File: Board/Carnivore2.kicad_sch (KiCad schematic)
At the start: 153 parts, among them J1 Conn_01x02_Pin, T1 2SC945, T2 2SA733, T3 2SC945, T4 2SC945, T5 2SC945, T6 2SA733, U7 50 MHz, U8 DNI, X1 EDGE50/MSX, X2 HEADER_5X2, X3 HEADER_5X2

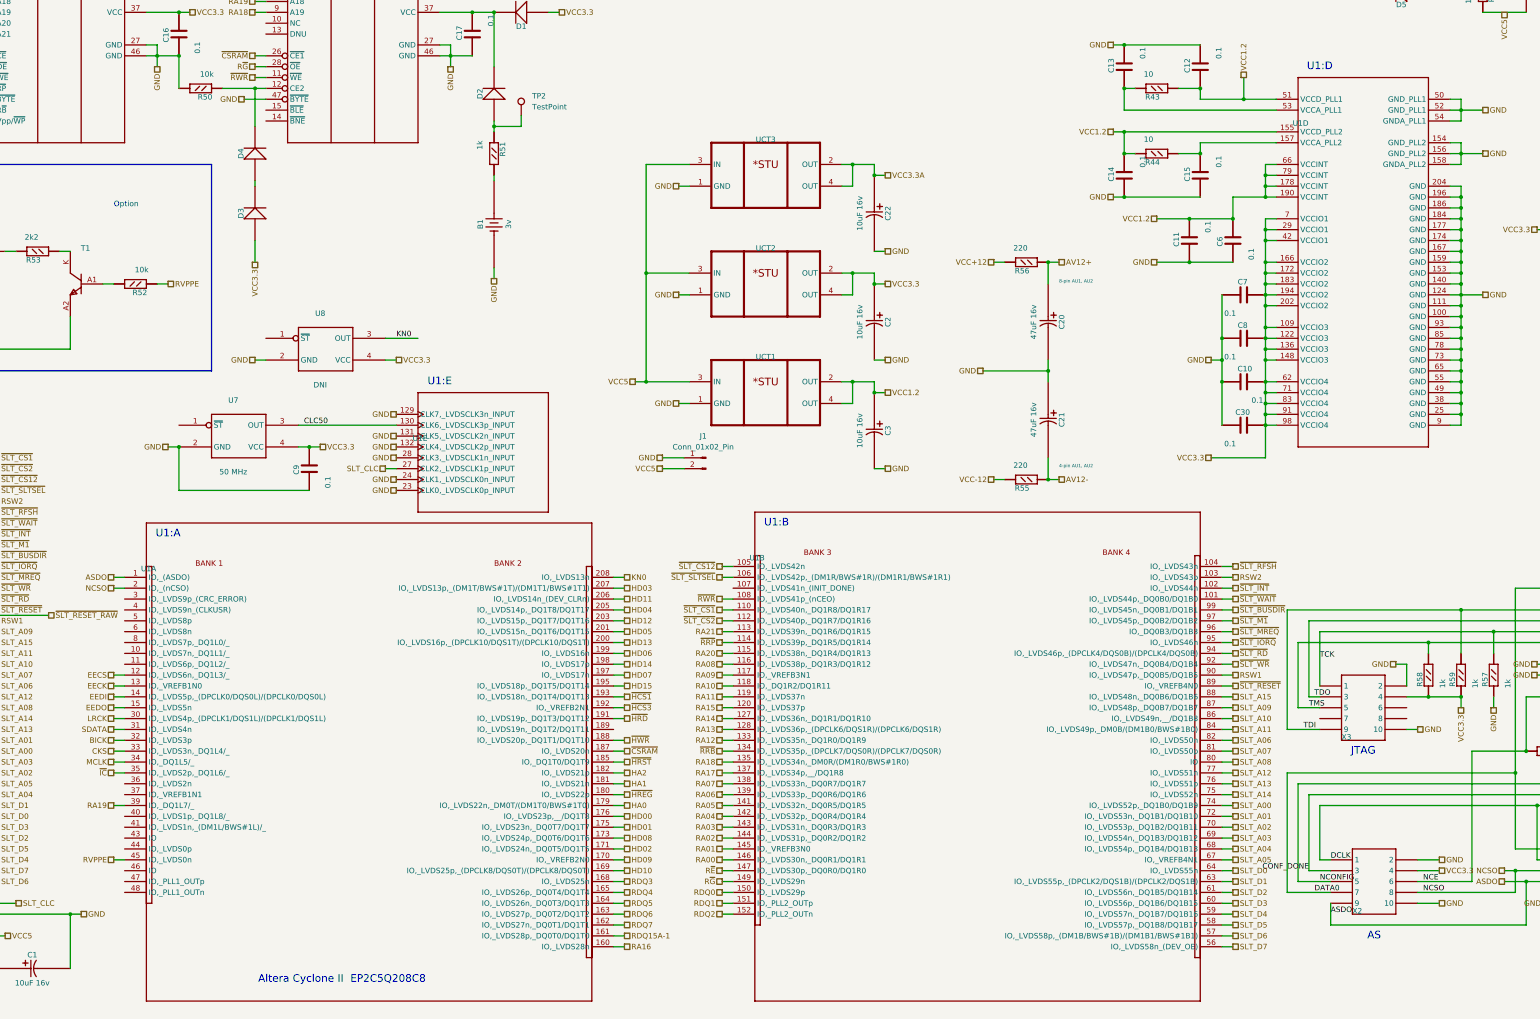
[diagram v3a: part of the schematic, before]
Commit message: Changed fpga from EP2C5 to EP2C8
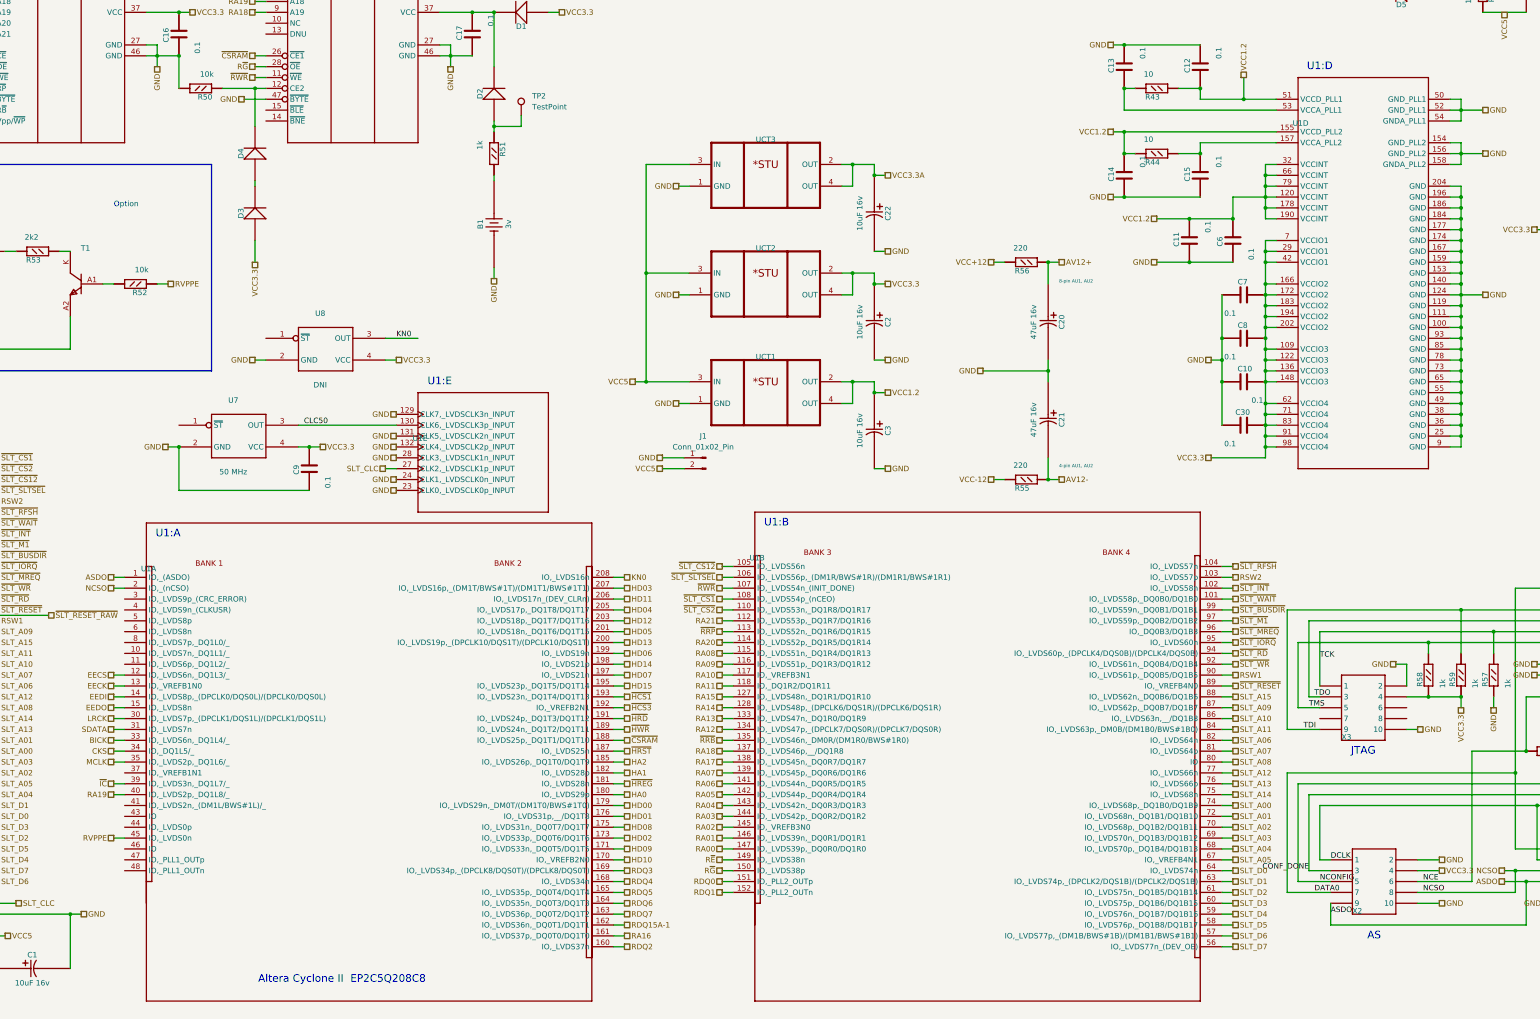
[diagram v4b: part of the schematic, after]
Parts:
- U1: footprint EP2C5Q208C8_1 -> EP2C8Q208C8_1; symbol Sheet1-altium-import:root_0_EP2C5Q208C8 -> Library:EP2C8Q208C8
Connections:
- net BICK: now also U1.33 (IO,_LVDS6n,_DQ1L4/_); no longer U1.32 (IO,_LVDS3p)
- net CKS: now also U1.34 (IO,_DQ1L5/_); no longer U1.33 (IO,_LVDS3n,_DQ1L4/_)
- net GND: now also U1.119 (GND), U1.36 (GND)
- net HA0: now also U1.180 (IO,_LVDS29p); no longer U1.179 (IO,_LVDS22n,_DM0T/(DM1T0/BWS#1T0))
- net HA1: now also U1.182 (IO,_LVDS28p); no longer U1.181 (IO,_LVDS21n)
- net HA2: now also U1.185 (IO,_LVDS26p,_DQ1T0/DQ1T9); no longer U1.182 (IO,_LVDS21p)
- net HD00: now also U1.179 (IO,_LVDS29n,_DM0T/(DM1T0/BWS#1T0)); no longer U1.176 (IO,_LVDS23p,__/DQ1T8)
- net HD01: now also U1.176 (IO,_LVDS31p,__/DQ1T8); no longer U1.175 (IO,_LVDS23n,_DQ0T7/DQ1T7)
- net HD02: now also U1.173 (IO,_LVDS33p,_DQ0T6/DQ1T6); no longer U1.171 (IO,_LVDS24n,_DQ0T5/DQ1T5)
- net HD08: now also U1.175 (IO,_LVDS31n,_DQ0T7/DQ1T7); no longer U1.173 (IO,_LVDS24p,_DQ0T6/DQ1T6)
- net HD09: now also U1.171 (IO,_LVDS33n,_DQ0T5/DQ1T5); no longer U1.170 (IO,_VREFB2N0)
- net HD10: now also U1.170 (IO,_VREFB2N0); no longer U1.169 (IO,_LVDS25p,_(DPCLK8/DQS0T)/(DPCLK8/DQS0T))
- net MCLK: now also U1.35 (IO,_LVDS2p,_DQ1L6/_); no longer U1.34 (IO,_DQ1L5/_)
- net RA00: now also U1.147 (IO,_LVDS39p,_DQ0R0/DQ1R0); no longer U1.146 (IO,_LVDS30n,_DQ0R1/DQ1R1)
- net RA01: now also U1.146 (IO,_LVDS39n,_DQ0R1/DQ1R1); no longer U1.145 (IO,_VREFB3N0)
- net RA02: now also U1.145 (IO,_VREFB3N0); no longer U1.144 (IO,_LVDS31p,_DQ0R2/DQ1R2)
- net RA03: now also U1.144 (IO,_LVDS42p,_DQ0R2/DQ1R2); no longer U1.143 (IO,_LVDS31n,_DQ0R3/DQ1R3)
- net RA04: now also U1.143 (IO,_LVDS42n,_DQ0R3/DQ1R3); no longer U1.142 (IO,_LVDS32p,_DQ0R4/DQ1R4)
- net RA05: now also U1.142 (IO,_LVDS44p,_DQ0R4/DQ1R4); no longer U1.141 (IO,_LVDS32n,_DQ0R5/DQ1R5)
- net RA06: now also U1.141 (IO,_LVDS44n,_DQ0R5/DQ1R5); no longer U1.139 (IO,_LVDS33p,_DQ0R6/DQ1R6)
- net RA07: now also U1.139 (IO,_LVDS45p,_DQ0R6/DQ1R6); no longer U1.138 (IO,_LVDS33n,_DQ0R7/DQ1R7)
- net RA08: now also U1.115 (IO,_LVDS51n,_DQ1R4/DQ1R13); no longer U1.116 (IO,_LVDS38p,_DQ1R3/DQ1R12)
- net RA09: now also U1.116 (IO,_LVDS51p,_DQ1R3/DQ1R12); no longer U1.117 (IO,_VREFB3N1)
- net RA10: now also U1.117 (IO,_VREFB3N1); no longer U1.118 (IO,_DQ1R2/DQ1R11)
- net RA11: now also U1.118 (IO,_DQ1R2/DQ1R11); no longer U1.119 (IO,_LVDS37n)
- net RA12: now also U1.134 (IO,_LVDS47p,_(DPCLK7/DQS0R)/(DPCLK7/DQS0R)); no longer U1.133 (IO,_LVDS35n,_DQ1R0/DQ1R9)
- net RA13: now also U1.133 (IO,_LVDS47n,_DQ1R0/DQ1R9); no longer U1.128 (IO,_LVDS36p,_(DPCLK6/DQS1R)/(DPCLK6/DQS1R))
- net RA14: now also U1.128 (IO,_LVDS48p,_(DPCLK6/DQS1R)/(DPCLK6/DQS1R)); no longer U1.127 (IO,_LVDS36n,_DQ1R1/DQ1R10)
- net RA15: now also U1.127 (IO,_LVDS48n,_DQ1R1/DQ1R10); no longer U1.120 (IO,_LVDS37p)
- net RA16: now also U1.161 (IO,_LVDS37p,_DQ0T0/DQ1T0); no longer U1.160 (IO,_LVDS28n)
- net RA17: now also U1.138 (IO,_LVDS45n,_DQ0R7/DQ1R7); no longer U1.137 (IO,_LVDS34p,__/DQ1R8)
- net RA18: now also U1.137 (IO,_LVDS46p,__/DQ1R8); no longer U1.135 (IO,_LVDS34n,_DM0R/(DM1R0/BWS#1R0))
- net RA19: now also U1.40 (IO,_LVDS2p,_DQ1L8/_); no longer U1.39 (IO,_DQ1L7/_)
- net RA20: now also U1.114 (IO,_LVDS52p,_DQ1R5/DQ1R14); no longer U1.115 (IO,_LVDS38n,_DQ1R4/DQ1R13)
- net RA21: now also U1.112 (IO,_LVDS53p,_DQ1R7/DQ1R16); no longer U1.113 (IO,_LVDS39n,_DQ1R6/DQ1R15)
- net RDQ0: now also U1.151 (IO,_PLL2_OUTp); no longer U1.150 (IO,_LVDS29p)
- net RDQ1: now also U1.152 (IO,_PLL2_OUTn); no longer U1.151 (IO,_PLL2_OUTp)
- net RDQ15A-1: now also U1.162 (IO,_LVDS36n,_DQ0T1/DQ1T1); no longer U1.161 (IO,_LVDS28p,_DQ0T0/DQ1T0)
- net RDQ2: now also U1.160 (IO,_LVDS37n); no longer U1.152 (IO,_PLL2_OUTn)
- net RDQ3: now also U1.169 (IO,_LVDS34p,_(DPCLK8/DQS0T)/(DPCLK8/DQS0T)); no longer U1.168 (IO,_LVDS25n)
- net RDQ4: now also U1.168 (IO,_LVDS34n); no longer U1.165 (IO,_LVDS26p,_DQ0T4/DQ1T4)
- net RDQ5: now also U1.165 (IO,_LVDS35p,_DQ0T4/DQ1T4); no longer U1.164 (IO,_LVDS26n,_DQ0T3/DQ1T3)
- net RDQ6: now also U1.164 (IO,_LVDS35n,_DQ0T3/DQ1T3); no longer U1.163 (IO,_LVDS27p,_DQ0T2/DQ1T2)
- net RDQ7: now also U1.163 (IO,_LVDS36p,_DQ0T2/DQ1T2); no longer U1.162 (IO,_LVDS27n,_DQ0T1/DQ1T1)
- net R~{E}: now also U1.149 (IO,_LVDS38n); no longer U1.147 (IO,_LVDS30p,_DQ0R0/DQ1R0)
- net R~{G}: now also U1.150 (IO,_LVDS38p); no longer U1.149 (IO,_LVDS29n)
- net VCC1.2: now also U1.120 (VCCINT), U1.32 (VCCINT)
- net ~{CSRAM}: now also U1.188 (IO,_LVDS25p,_DQ1T1/DQ1T10); no longer U1.187 (IO,_LVDS20n)
- net ~{HREG}: now also U1.181 (IO,_LVDS28n); no longer U1.180 (IO,_LVDS22p)
- net ~{HRST}: now also U1.187 (IO,_LVDS25n); no longer U1.185 (IO,_DQ1T0/DQ1T9)
- net ~{HWR}: now also U1.189 (IO,_LVDS24n,_DQ1T2/DQ1T11); no longer U1.188 (IO,_LVDS20p,_DQ1T1/DQ1T10)
- net ~{IC}: now also U1.39 (IO,_LVDS3n,_DQ1L7/_); no longer U1.35 (IO,_LVDS2p,_DQ1L6/_)
- net ~{RRB}: now also U1.135 (IO,_LVDS46n,_DM0R/(DM1R0/BWS#1R0)); no longer U1.134 (IO,_LVDS35p,_(DPCLK7/DQS0R)/(DPCLK7/DQS0R))
- net ~{RRP}: now also U1.113 (IO,_LVDS52n,_DQ1R6/DQ1R15); no longer U1.114 (IO,_LVDS39p,_DQ1R5/DQ1R14)
- net ~{RWR}: now also U1.107 (IO,_LVDS54n_(INIT_DONE)); no longer U1.108 (IO,_LVDS41p_(nCEO))
- net ~{SLT_CS1}: now also U1.108 (IO,_LVDS54p_(nCEO)); no longer U1.110 (IO,_LVDS40n,_DQ1R8/DQ1R17)
- net ~{SLT_CS2}: now also U1.110 (IO,_LVDS53n,_DQ1R8/DQ1R17); no longer U1.112 (IO,_LVDS40p,_DQ1R7/DQ1R16)

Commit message: Changed audio DAC to modern type, added audio input, updated footprints
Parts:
- removed AU1: ~, 4558D_1, symbol Sheet1-altium-import:root_2_mirrored_4558D
- removed AU2: ~, 4558D_1, symbol Sheet1-altium-import:root_0_4558D
- removed C18: 0.1mk, C_0603_1, symbol Sheet1-altium-import:root_0_C_0805
- removed C19: 0.1mk, C_0603_1, symbol Sheet1-altium-import:root_1_C_0805
- removed C20, C21: 100mk 16v, C_1812_1, symbol Sheet1-altium-import:root_3_CAP100RP
- removed C202: 1n, C_0603_1, symbol Sheet1-altium-import:root_1_C_0805
- removed D5: 1N4148, DIODE_1N4148_1, symbol Sheet1-altium-import:root_2_DIODE
- removed D6: 1N4148, DIODE_1N4148_1, symbol Sheet1-altium-import:root_1_DIODE
- removed R101, R201, R52: 10k, R_0603_1, symbol Sheet1-altium-import:root_2_R_0805
- removed R102, R202: 4.7k, R_0603_1, symbol Sheet1-altium-import:root_2_R_0805
- removed R105, R205: 1.8k, R_0603_1, symbol Sheet1-altium-import:root_2_R_0805
- removed R106, R206: 1k, R_0603_1, symbol Sheet1-altium-import:root_2_R_0805
- removed R53, R62, R63: 2.2k, R_0603_1, symbol Sheet1-altium-import:root_2_R_0805
- removed R54: 10, R_0603_1, symbol Sheet1-altium-import:root_3_R_0805
- removed R55, R56: 220, R_0603_1, symbol Sheet1-altium-import:root_2_R_0805
- removed R65: 10k, R_0603_1, symbol Sheet1-altium-import:root_3_R_0805
- removed T1: 2SC945, SOT-23(A1A2K)_1, symbol Sheet1-altium-import:root_0_mirrored_NPN
- removed T2: 2SA733, SOT-23(A1A2K)_1, symbol Sheet1-altium-import:root_2_PNP
- removed T3, T4, T5: 2SC945, SOT-23(A1A2K)_1, symbol Sheet1-altium-import:root_2_mirrored_NPN
- removed T6: 2SA733, SOT-23(A1A2K)_1, symbol Sheet1-altium-import:root_2_mirrored_PNP
- removed U5: ~, YAC516-E_1, symbol Sheet1-altium-import:root_0_YAC516-E
- removed U8: DNI, Oscillator:Oscillator_SMD_TXC_7C-4Pin_5.0x3.2mm_HandSoldering, symbol Sheet1-altium-import:root_0_SG-310
- added AX2: {Value}, Library:ST-222_1, symbol Sheet1-altium-import:root_0_mirrored_ST-222
- added C31, C32, C33, C34, C35: 100nF, Library:C_0603_1, symbol Sheet1-altium-import:root_1_C_0805
- added C36: 2.2nF, Library:C_0603_1, symbol Sheet1-altium-import:root_1_C_0805
- added J2: Conn_01x03_Pin, Connector_PinHeader_2.54mm:PinHeader_1x03_P2.54mm_Vertical, symbol Connector:Conn_01x03_Pin
- added R49: 470, Library:R_0603_1, symbol Sheet1-altium-import:root_2_R_0805
- added R99: 10, Library:R_0603_1, symbol Sheet1-altium-import:root_2_R_0805
- added U5: ~, Package_SO:TSSOP-20_4.4x6.5mm_P0.65mm, symbol Library:PCM510xA
- added U9: ~, Package_SO:TSSOP-14_4.4x5mm_P0.65mm, symbol Library:PCM1808
- AX1: footprint ST-222_1 -> Library:ST-222_1
- B1: footprint (none) -> Library:BAT
- C1, C2, C22, C3, C4: footprint C_1812_1 -> Library:C_1812_1
- C10, C11, C12, C13, C14, C15, C16, C17, C30, C5, C6, C7, C8, C9, LED1: footprint C_0603_1 -> Library:C_0603_1
- C101, C201: value 1n -> 2.2nF; footprint C_0603_1 -> Library:C_0603_1; ALTIUM_VALUE 1n -> (none)
- C102: value 1n -> 100nF; footprint C_0603_1 -> Library:C_0603_1; ALTIUM_VALUE 1n -> (none)
- C103, C105, C203, C205: value 4.7mk 25v -> 10uF 16V; footprint C_1206_1 -> Library:C_1206_1; ALTIUM_VALUE 4,7uF 25v -> (none)
- C104, C204: value 390p -> 2.2uF; footprint C_0603_1 -> Library:C_0603_1; ALTIUM_VALUE 390p -> (none)
- C23: value 10mk -> 10uF 16V; footprint C_1812_1 -> Library:C_1812_1; ALTIUM_VALUE 10uF 16v -> (none)
- C24, C25, C27: value 0.1mk -> 100nF; footprint C_0603_1 -> Library:C_0603_1; ALTIUM_VALUE 0.1 -> (none)
- C26: value 10mk -> 10uF 16V; footprint C_1812_1 -> Library:C_1812_1; ALTIUM_VALUE 10uF16v -> (none)
- C28: value 10mk -> 10uF 16v; footprint C_1812_1 -> Library:C_1812_1; ALTIUM_VALUE 10uF 10v -> (none)
- C29: value 22mk -> 10uF 16V; footprint C_1812_1 -> Library:C_1812_1; ALTIUM_VALUE 22uF 10v -> (none)
- D1, D2, D3, D4: footprint DIODE_1N4148_1 -> Library:DIODE_1N4148_1
- H1, H2: footprint (none) -> Library:MountingHole
- J1: footprint JUMPER_1 -> Library:JUMPER_1
- R10, R11, R12, R13, R14, R15, R16, R17, R18, R19, R2, R20, R21, R22, R23, R24, R25, R26, R27, R28, R29, R3, R30, R31, R32, R33, R34, R35, R36, R37, R38, R39, R4, R40, R41, R42, R5, R6, R7, R8, R9: footprint C0603_1 -> Library:R_0603_1
- R103, R203, R43, R44, R45, R46, R47, R48, R50, R51, R57, R58, R59, R64, R66: footprint R_0603_1 -> Library:R_0603_1
- R104, R204: value 100k -> 470; footprint R_0603_1 -> Library:R_0603_1; ALTIUM_VALUE 100k -> (none)
- R60: value 10k -> 470; footprint R_0603_1 -> Library:R_0603_1; ALTIUM_VALUE 10K -> (none)
- R61: value 2.2k -> 470; footprint R_0603_1 -> Library:R_0603_1; ALTIUM_VALUE 2k2 -> (none)
- TP1, TP2: footprint (none) -> Library:TestPoint_THTPad_D1.5mm_Drill0.9mm
- U1: footprint EP2C8Q208C8_1 -> Library:EP2C5Q208C8_1
- U2: footprint M29W320DXXXNXX_1 -> Library:M29W320DXXXNXX_1
- U3: footprint CY62167DV30_1 -> Library:CY62167DV30_1
- U4: footprint EPCS4SI8_1 -> Package_SO:SO-8_3.9x4.9mm_P1.27mm; symbol Sheet1-altium-import:root_0_EPCS4SI8 -> Library:M25P80-VMN
- U6: footprint M93C46MN1_1 -> Package_SO:SO-8_3.9x4.9mm_P1.27mm; symbol Sheet1-altium-import:root_0_93C46DSM -> Library:AT93C46DN
- U7: footprint SG-310_1 -> Library:SG-310_1
- UCT1, UCT2, UCT3: footprint ADP3338_1 -> Library:ADP3338_1
- X1: footprint EDGE50/MSX_1 -> Library:EDGE50_MSX_1
- X2, X3: footprint HDR2X5 -> Library:HDR2X5
- XC1: footprint CF-50-001_1 -> Library:CF-50-001_1
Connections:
- net CONF_DONE: no longer R47.1, U1.123 (CONF_DONE), X2.3
- net GND: now also C102.1, C205.2 (MINUS), C34.1, J2.1 (Pin_1), R99.1, U5.16 (FMT), U5.19 (DGND), U9.12 (FMT), U9.5 (DGND); no longer AX1.1, AX1.M (Mount), C101.1, C102.2, C201.1, C24.1, C26.1 (MINUS), C27.1, C28.1 (MINUS), C29.1 (MINUS)
- net RVPPE: now also U1.43 (IO), U2.14 (Vpp/~{WP}); no longer U1.45 (IO,_LVDS0n)
- net SLTSOUND: now also R61.2
- net VCC3.3: now also C34.2, U9.4 (VDD)
- net VCC3.3A: now also C105.1 (PLUS), U5.8 (AVDD)
- net VCC5: now also C29.2 (PLUS), C35.2, U9.3 (VCC)
- net at R203.1: now also C33.2, U9.13 (VinL)
- net at C101.2: now also AX1.4, AX1.5, R104.2
- net at R61.1: now also R60.2, C36.1, R49.2
- net ADC_LRCK: now reaches U1.10 (IO,_LVDS7n,_DQ1L1/_)
- net ADC_LRCK: now also U9.7 (LRCK)
- net ADC_MD0: now reaches U1.3 (IO,_LVDS9p_(CRC_ERROR))
- net ADC_MD0: now also U9.10 (MD0)
- net DAC_FLT: now reaches U1.37 (IO,_VREFB1N1)
- net DAC_FLT: now also U5.11 (FLT)
- net ADC_DOUT: now reaches U1.4 (IO,_LVDS9n_(CLKUSR))
- net ADC_DOUT: now also U9.9 (DOUT)
- net at U1.44 (IO,_LVDS0p): now also J2.2 (Pin_2)
- net ADC_BCK: now reaches U1.5 (IO,_LVDS8p)
- net ADC_BCK: now also U9.8 (BCK)
- net ADC_SCKI: now reaches U1.8 (IO,_LVDS7p,_DQ1L0/_)
- net ADC_SCKI: now also U9.6 (SCKI)
- net at C26.2 (PLUS), C27.2: now also U5.1 (CPVDD)
- net at C23.2 (PLUS), C25.2, R64.1: now also U5.20 (DVDD)
- net at C28.2 (PLUS): now also C31.2, U9.1 (VREF); no longer R60.1
- net at AX1.2, AX1.3: now also C201.1, R204.2
- net at R103.1: now also C32.2, U9.14 (VinR); no longer C102.1
- net AGND: now reaches C105.2 (MINUS)
- net AGND: now also AX1.1, AX1.M (Mount), C101.1, C104.2, C201.2, C24.1, C26.1 (MINUS), C27.1, C28.1 (MINUS), C29.1 (MINUS), AX2.1, AX2.M (Mount), C31.1, C32.1, C33.1, C35.1, C36.2, R99.2, U5.3 (CPGND), U5.9 (AGND), U9.2 (AGND)
- net BICK renamed DAC_DIN
- net DAC_DIN: now also U5.14 (DIN)
- net CKS renamed DAC_BCK
- net DAC_BCK: now also U5.13 (BCK)
- net KN0 renamed ADC_MD1
- net ADC_MD1: now also U9.11 (MD1)
- net LRCK renamed DAC_XSMT
- net DAC_XSMT: now also U5.17 (XSMT)
- net MCLK renamed DAC_SCK
- net DAC_SCK: now also U5.12 (SCK)
- net SDATA renamed DAC_LRCK
- net DAC_LRCK: now also U5.15 (LRCK)
- net VCC+12: no longer names the net of X1.48
- net VCC-12: no longer names the net of X1.50
- net ~{IC} renamed DAC_DEMP
- net DAC_DEMP: now also U5.10 (DEMP)
- net ~{SLT_RESET_RAW}: no longer names the net of R30.2, X1.15
- new net: J2.3 (Pin_3), U1.45 (IO,_LVDS0n)
- new net: C102.2, C205.1 (PLUS), U5.18 (LDOO)
- new net: AX2.4, AX2.5, C103.2 (MINUS)
- new net: C204.1, U5.2 (CAPP)
- new net: C204.2, U5.4 (CAPM)
- new net: R204.1, R60.1, U5.7 (OUTR)
- new net: AX2.2, AX2.3, C203.2 (MINUS)
- new net: R104.1, R49.1, U5.6 (OUTL)
- new net: R47.1, U1.123 (CONF_DONE), X2.3
- new net: C104.1, U5.5 (VNEG)
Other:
- note added: "Audio In"
- note added: "Audio Out"
- note added: "EEPROM"
- note removed: "4-pin AU1, AU2"
- note removed: "8-pin AU1, AU2"
- note removed: "EPCS4SI8"
- note removed: "Option"
- note removed: "Option 93C46"
- note removed: "U4"
- note removed: "U6"
- moved on the sheet: AX1, C1, C101, C102, C103, C104, C105, C201, C203, C204, C205, C23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
